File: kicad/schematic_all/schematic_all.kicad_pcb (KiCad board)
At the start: 2 copper layers, 88.9 x 88.9 mm, 40 parts, among them J1 Power In, SW1 Button 1, SW2 Encoder 1, SW3 Button 2, SW4 Encoder 2, SW5 Button 3, U1 L7805, U2 RPi_Pico, U3 RDA5807M_Module, U4 LM386

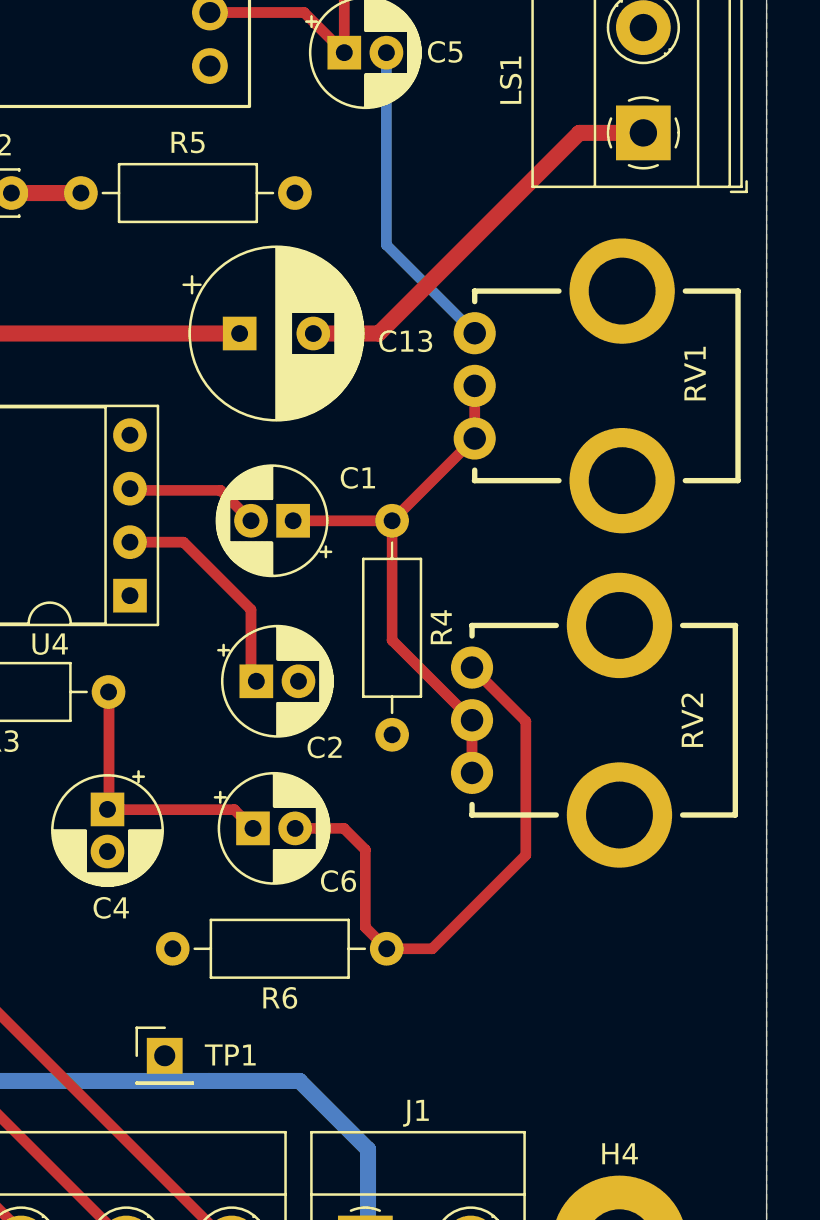
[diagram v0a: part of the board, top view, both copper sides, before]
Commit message: Minor changes & Added additional testpoints
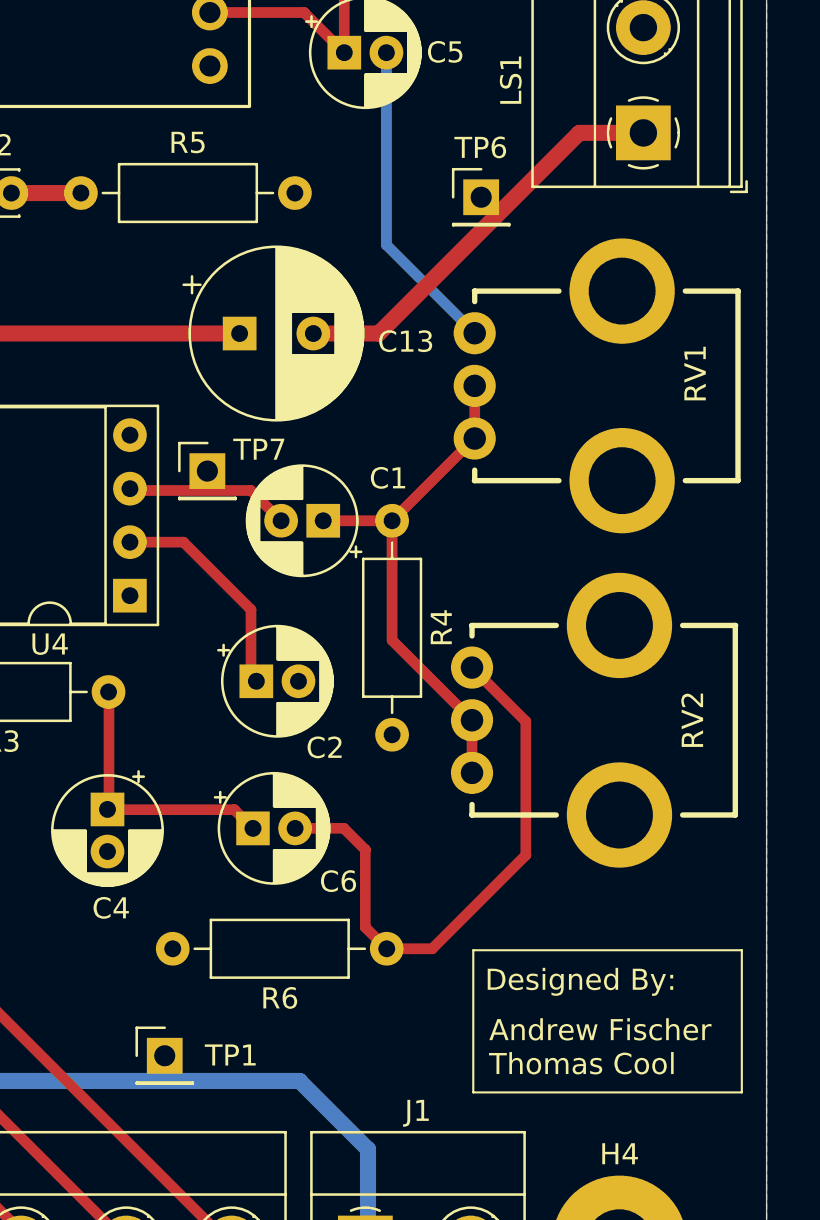
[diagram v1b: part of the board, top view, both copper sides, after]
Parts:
- added TP6: TestPoint, Connector_PinHeader_2.54mm:PinHeader_1x01_P2.54mm_Vertical, F.Cu at (132.5, 71.0)
- added TP7: TestPoint, Connector_PinHeader_2.54mm:PinHeader_1x01_P2.54mm_Vertical, F.Cu at (119.5, 84.0)
- moved C1 1.43 mm to (125.0, 86.4)
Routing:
- net Net-(U4-+): track 6.38 -> 7.81 mm
- net Net-(C1-Pad1): track 26.3 -> 24.9 mm
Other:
- board text added: "Andrew Fischer Thomas Cool"
- board text added: "Designed By:"

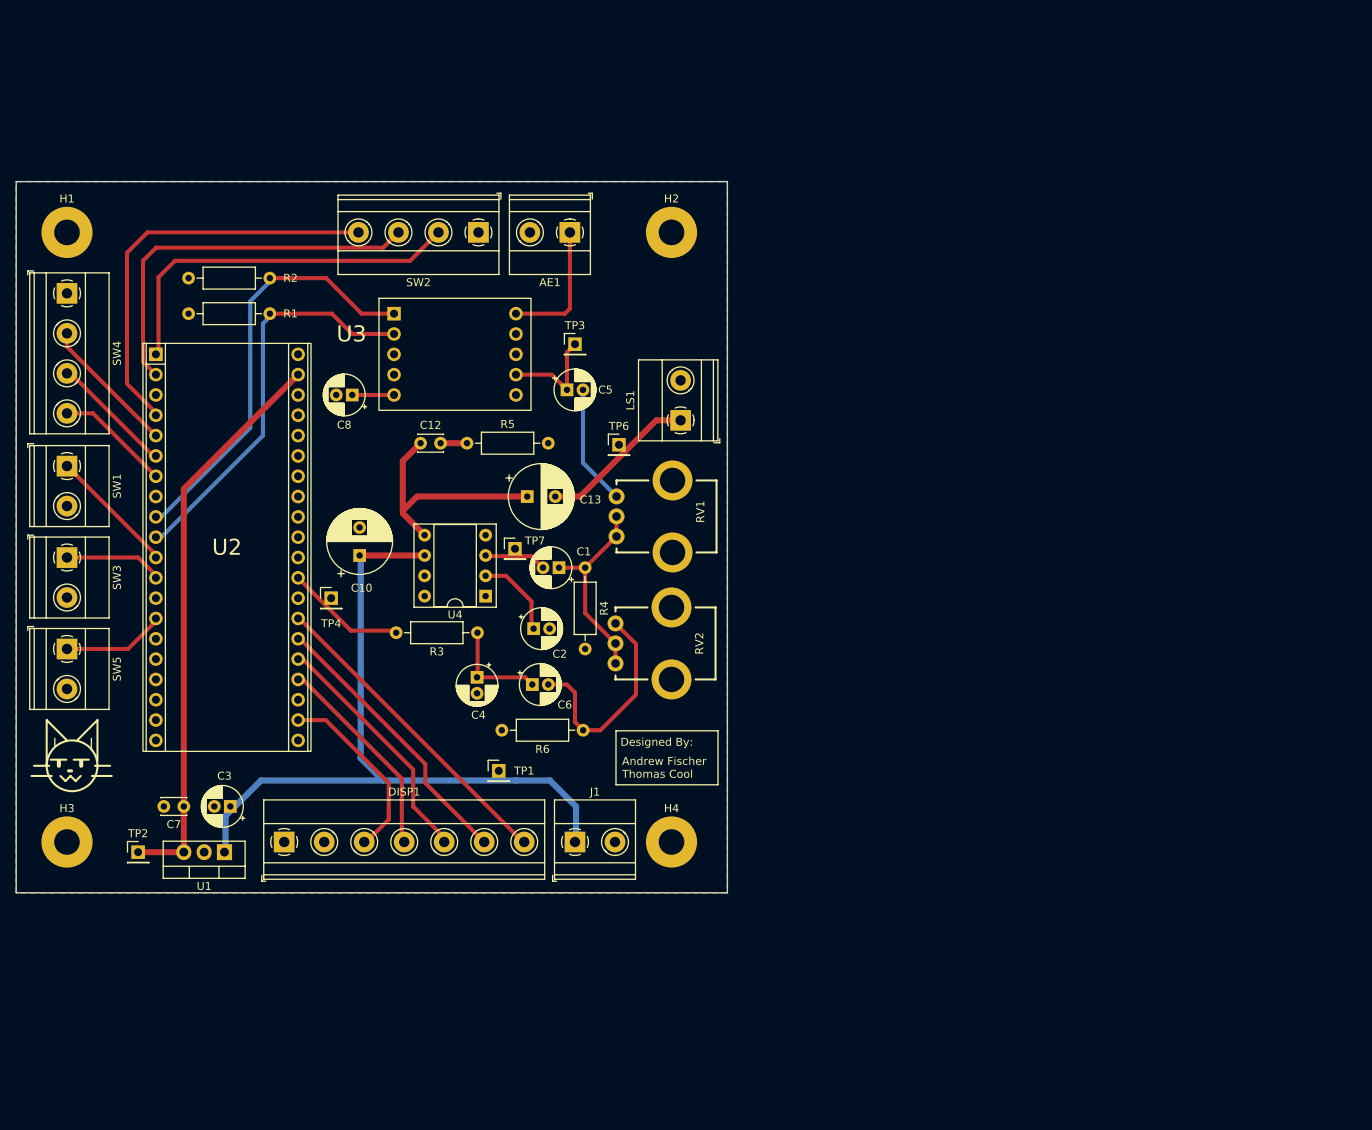
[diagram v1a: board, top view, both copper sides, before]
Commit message: adjustments on test points and ink
move speaker test point to before capacitor
increase size of designed by text
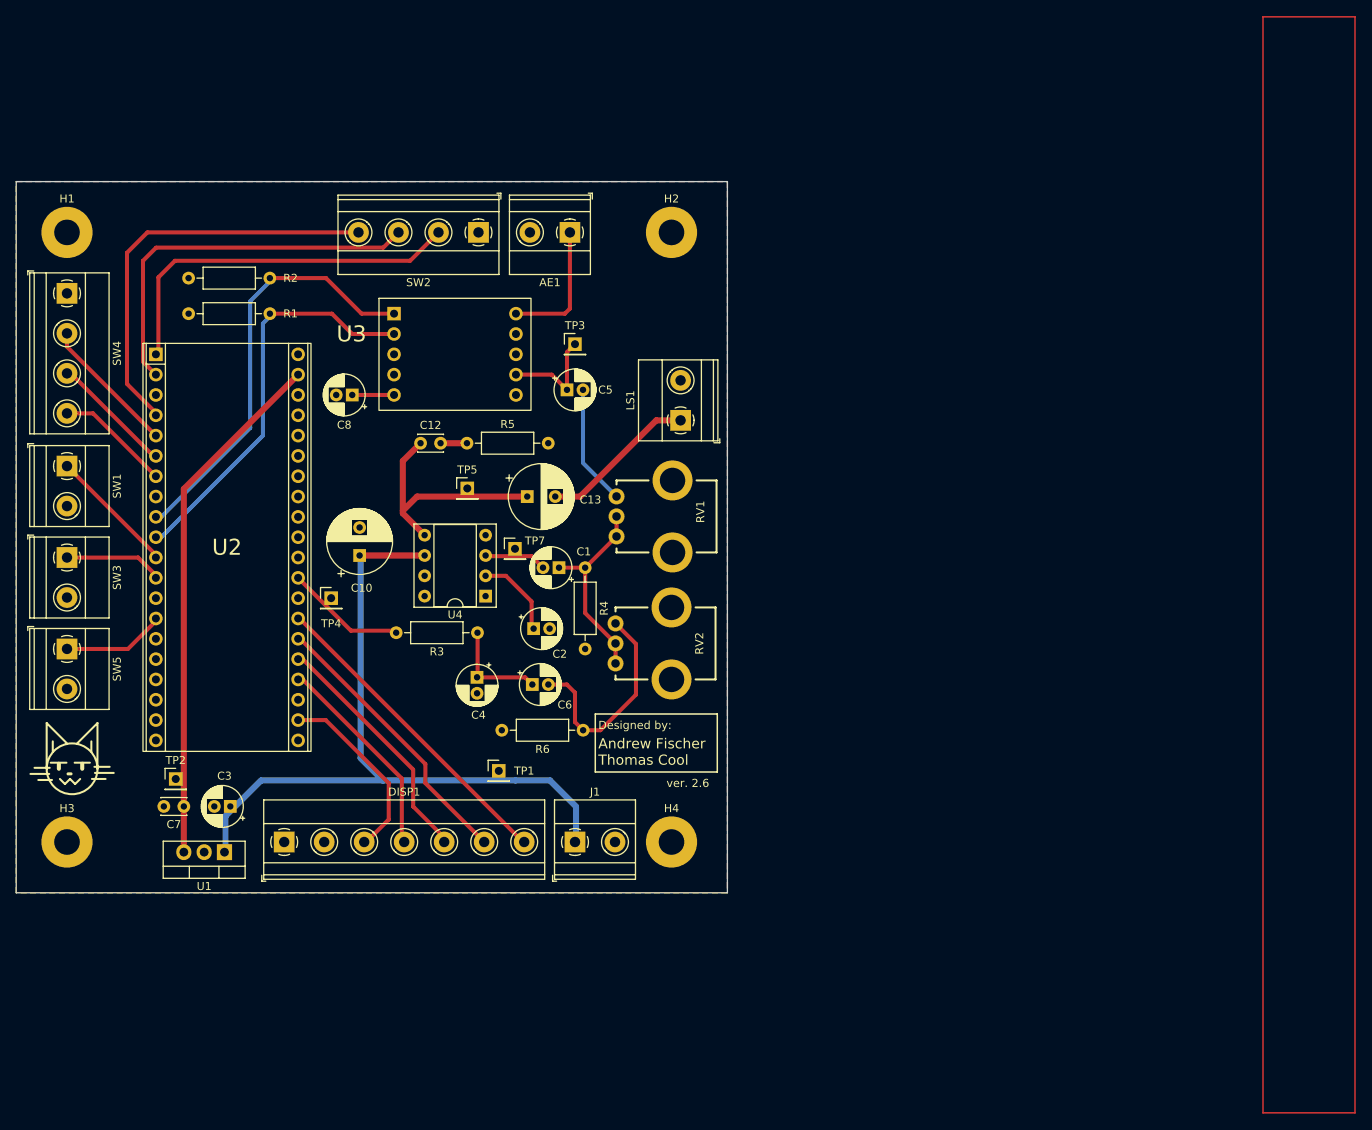
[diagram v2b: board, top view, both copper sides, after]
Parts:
- removed TP6: TestPoint, Connector_PinHeader_2.54mm:PinHeader_1x01_P2.54mm_Vertical
- added TP5: TestPoint, Connector_PinHeader_2.54mm:PinHeader_1x01_P2.54mm_Vertical, F.Cu at (113.5, 76.5)
- moved TP2 10.3 mm to (77.1, 112.8)
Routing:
- net +5V: track 71.3 -> 65.6 mm
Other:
- board text added: "Designed by:"
- board text added: "ver. 2.6"
- board text removed: "Designed By:"
